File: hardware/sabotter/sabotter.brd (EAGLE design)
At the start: 100 x 80 mm, 96 parts, among them IC1 MAX3232CSE, IC2 MAX3232CSE, IC3 OKI-78SR-3.3/1.5-W36H-C, IC4 OKI-78SR-5/1.5-W36H-C, IC6 ATXMEGA256A3U-AU

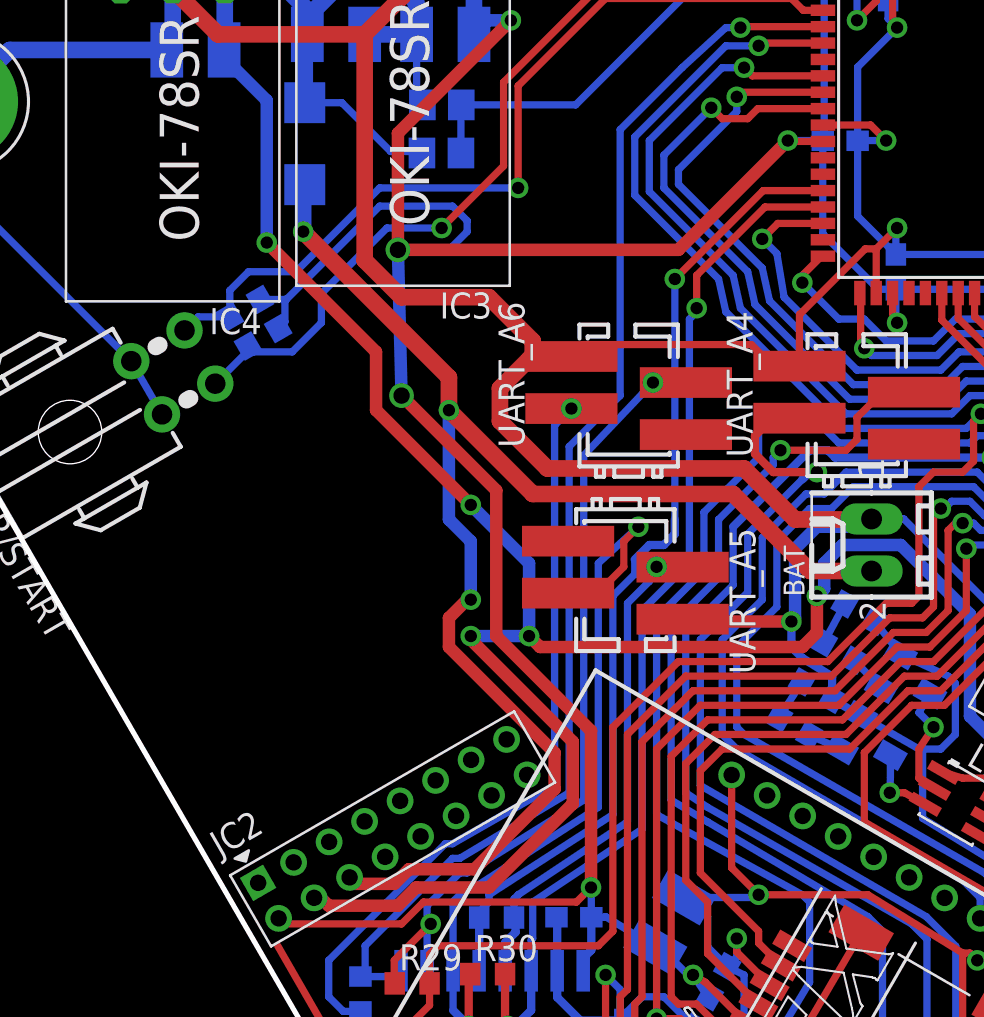
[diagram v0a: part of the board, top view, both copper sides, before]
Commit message: add audio amplifier
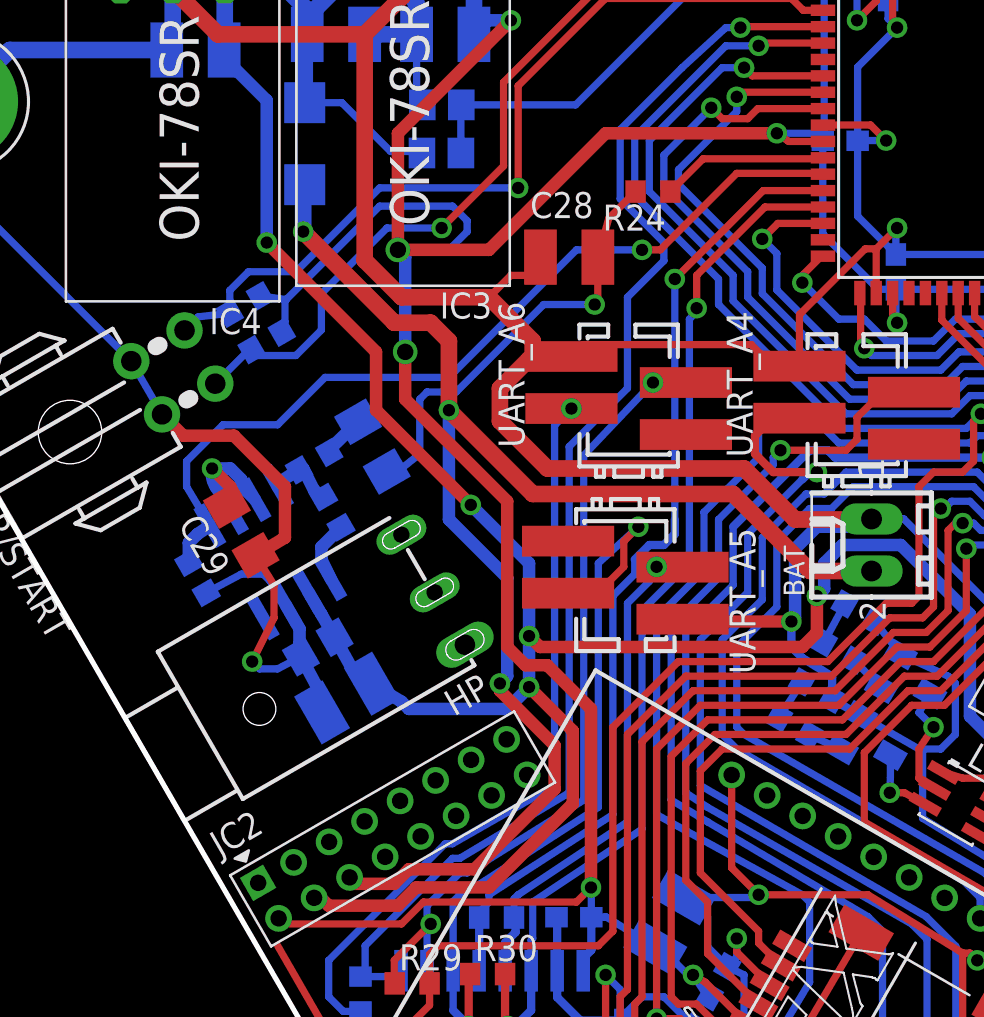
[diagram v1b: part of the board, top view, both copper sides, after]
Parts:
- added C27, C29: 1UF_50V_1206, robotter_capacitor:C1206
- added C28, C30: C_10UF, robotter_capacitor:C1210
- added C31: 100NF_50V_0805, robotter_capacitor:C0805
- added HP: 1503_04, con-lumberg:1503_04
- added IC7: LM4871M, robotter_ic:SO8
- added R24, R25, R37, R38: 10K-F, robotter_resistor:R0603
- C13, C14, C15, C16, C2: value 10UF35V-C -> 10UFC
- moved R2 0.25 mm to (23.3, 60.1)
- moved R3 0.18 mm to (22.2, 61.9)
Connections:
- new net AUDIO_PWM_3V3: IC6.26, R24.1
- new net ENABLE_AUDIO_OUPUT_3V3: IC6.27, IC7.1, R38.2
- new net N$15: C29.2, IC7.2, IC7.3
- new net N$20: C27.1, C28.2, R24.2
- new net N$36: C27.2, R25.1
- new net N$37: IC7.4, R25.2, R37.1
- new net N$38: IC7.5, R37.2
- net +5V: now also C30.1, C31.1, IC7.6
- net GND: now also C28.1, C29.1, C30.2, C31.2, IC7.7, R38.1
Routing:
- net ENABLE_AUDIO_OUPUT_3V3: track 0.00 -> 42.7 mm, vias 0 -> 1
- net GND: track 512.6 -> 546.9 mm, vias 18 -> 19
- net N$20: track 0.00 -> 21.2 mm, vias 0 -> 1
- net +5V: track 113.5 -> 123.6 mm
- net AUDIO_PWM_3V3: track 0.00 -> 8.13 mm
- net N$15: track 0.00 -> 7.57 mm, vias 0 -> 1
- net N$37: track 0.00 -> 3.37 mm
- net N$38: track 0.00 -> 3.02 mm
- net N$36: track 0.00 -> 2.11 mm
- net +3V3: track 259.8 -> 261.7 mm
- net RX_A6_3V3: track 62.3 -> 64.0 mm

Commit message: board ready for eirbot assembly
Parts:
- removed LED3, LED4, LED5: GREEN_0805, robotter_diode:CHIP-LED0805
- added LA1, LA3, LA4: GREEN_0805, robotter_diode:CHIP-LED0805
- added R39, R40, R41, R42: 10K-F, robotter_resistor:R0603
- moved LED9 61.7 mm to (4.17, 67.8), turned to 30 degrees
- moved LED6 60.5 mm to (9.40, 60.3)
- moved LED7 60.5 mm to (8.14, 62.7)
- moved LED8 60.5 mm to (6.91, 65.0)
- moved R8 59.4 mm to (14.4, 61.5), turned to 180 degrees
- moved R10 59.1 mm to (11.8, 65.8), turned to 180 degrees
- moved R9 59.0 mm to (13.1, 63.7), turned to 180 degrees
- moved R11 57.8 mm to (13.2, 67.9), turned to 180 degrees
- moved R5 1.83 mm to (70.7, 41.7)
- moved R4 1.12 mm to (72.9, 43.7)
- moved R6 0.40 mm to (68.4, 33.5)
- moved R7 0.18 mm to (67.0, 31.1)
- renumbered LED2 to LA2, UART_A4 to UART_E0, UART_A5 to UART_D0, UART_A6 to UART_C0
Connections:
- net RX_A4_232 renamed RX_E0_232
- net RX_A5_232 renamed RX_D0_232
- net RX_A6_232 renamed RX_C0_232
- net TX_A4_232 renamed TX_E0_232
- net TX_A4_3V3 renamed TX_E0_3V3
- net TX_A5_232 renamed TX_D0_232
- net TX_A5_3V3 renamed TX_D0_3V3
- net TX_A6_232 renamed TX_C0_232
- net TX_A6_3V3 renamed TX_C0_3V3
- removed net N$10: LED4.A
- removed net N$11: LED7.C, R9.2
- removed net N$12: LED5.A
- removed net N$74: IC6.1
- removed net N$77: IC6.2
- removed net N$78: IC6.3
- removed net N$79: IC6.4
- removed net N$80: IC6.5
- removed net N$9: LED3.A
- removed net RX_A4_3V3: IC1.12, IC6.38, R26.2
- removed net RX_A5_3V3: IC2.12, IC6.28, R27.2
- removed net RX_A6_3V3: IC2.9, IC6.18, R28.2
- new net LA1: IC6.63, R5.2
- new net LA2: IC6.64, R4.2
- new net LA3: IC6.1, R7.2
- new net LA4: IC6.2, R6.2
- new net RX_C0_3V3: IC2.9, IC6.18, R28.2, R39.2
- new net RX_D0_3V3: IC2.12, IC6.28, R27.2, R40.2
- new net RX_E0_3V3: IC1.12, IC6.38, R26.2, R41.2
- net GND: now also LA1.C, LA2.C, LA3.C, LA4.C, LED6.C, LED7.C, LED8.C, LED9.C, R39.1, R40.1, R41.1, R42.1; no longer R10.1, R11.1, R4.1, R5.1, R6.1, R7.1, R8.1, R9.1
- net N$1: now also LA2.A, R4.1; no longer LA2.C, R4.2
- net N$13: now also R8.2; no longer LED6.A
- net N$14: now also R9.2; no longer LED7.A
- net N$16: now also R10.2; no longer LED8.A
- net N$17: now also R11.2; no longer LED9.A
- net N$2: now also LA1.A, R5.1; no longer LED3.C, R5.2
- net N$3: now also LED6.A, R8.1; no longer LED4.C, R6.2
- net N$4: now also LA3.A, R7.1; no longer LED5.C, R7.2
- net N$5: now also LED7.A, R9.1; no longer LED6.C, R8.2
- net N$6: now also LED8.A, R10.1; no longer LED8.C, R10.2
- net N$7: now also LED9.A, R11.1; no longer LED9.C, R11.2
- net N$8: now also LA4.A, R6.1; no longer LA2.A
- net RX_PROP_3V3: now also R42.2
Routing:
- net LA3: track 0.00 -> 70.5 mm, vias 0 -> 1
- net LA4: track 0.00 -> 69.9 mm, vias 0 -> 1
- net RX_C0_3V3: track 0.00 -> 66.7 mm, vias 0 -> 1
- net RX_A6_3V3: track 64.0 -> 0.00 mm, vias 1 -> 0
- net RX_E0_3V3: track 0.00 -> 60.9 mm, vias 0 -> 1
- net RX_A4_3V3: track 60.6 -> 0.00 mm, vias 1 -> 0
- net LA1: track 0.00 -> 53.0 mm, vias 0 -> 1
- net LA2: track 0.00 -> 52.2 mm, vias 0 -> 1
- net RX_D0_3V3: track 0.00 -> 48.4 mm, vias 0 -> 1
- net RX_A5_3V3: track 47.9 -> 0.00 mm, vias 1 -> 0
- net GND: track 546.9 -> 584.4 mm, vias 19 -> 23
- net N$2: track 0.00 -> 7.28 mm, vias 0 -> 1
- net RX_PROP_3V3: track 24.7 -> 29.9 mm
- net N$7: track 3.59 -> 8.28 mm
- net N$1: track 0.00 -> 3.58 mm, vias 0 -> 1
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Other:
- board text added: "Sab'Otter V1"

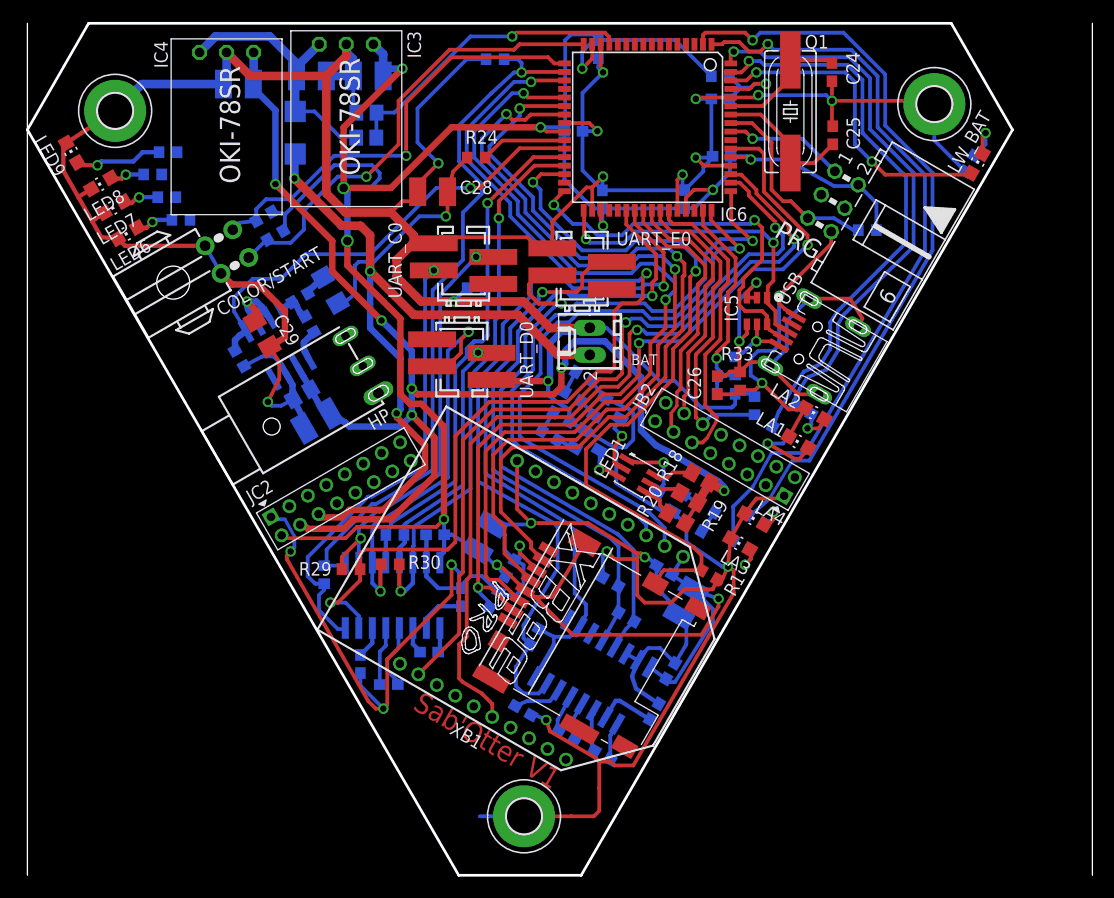
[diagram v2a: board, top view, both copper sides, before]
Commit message: board ready for eirbot assembly, sabotter V1
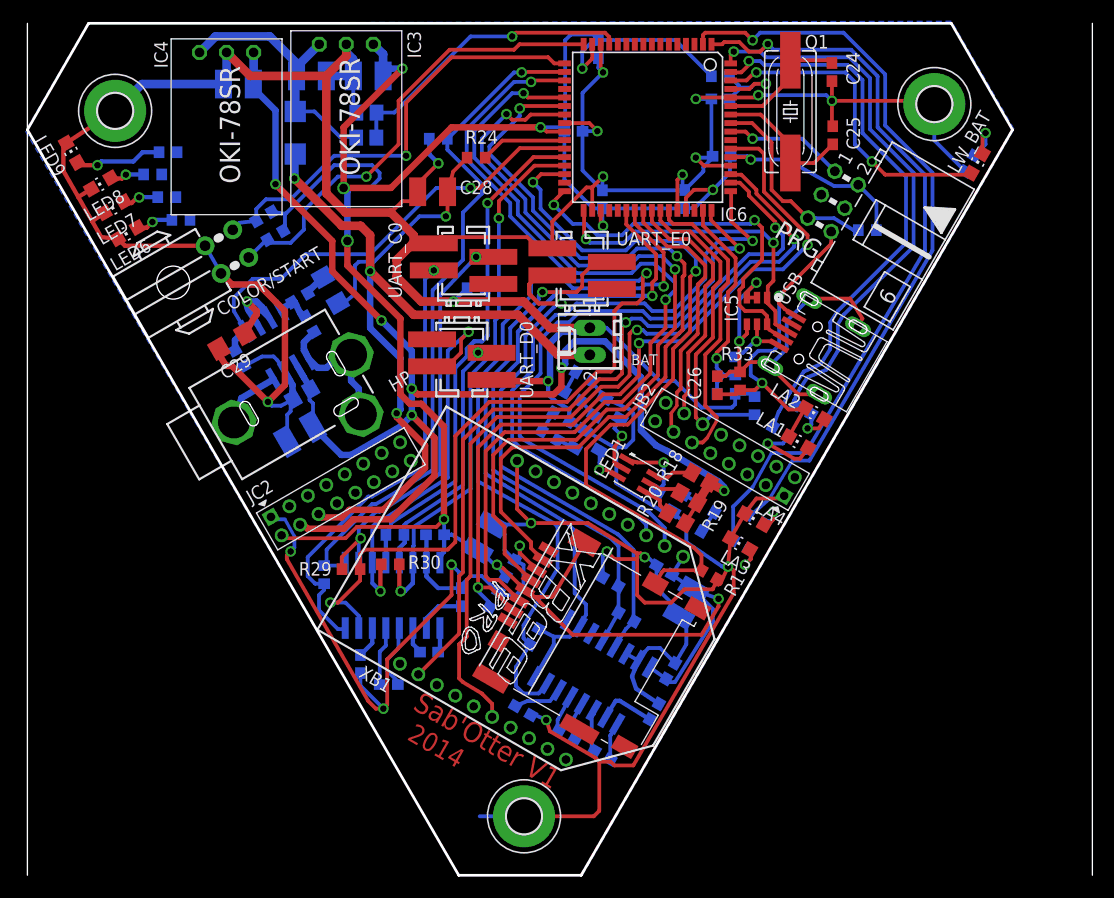
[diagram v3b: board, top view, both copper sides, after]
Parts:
- HP: value 1503_04 -> 1503_12"; device con-lumberg:1503_04 -> robotter_connector:1503_12
- moved R39 9.18 mm to (38.6, 69.2)
- moved HP 4.06 mm to (24.9, 45.7)
- moved C29 2.93 mm to (19.2, 50.1), turned to 30 degrees
- moved C30 2.03 mm to (25.6, 41.4)
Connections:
- net N$13 renamed LED4
- net N$14 renamed LED3
- net N$16 renamed LED2
- net N$17 renamed LED1
- new net N$9: HP.5, IC7.8
- net N$38: now also HP.3, HP.4
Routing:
- net N$38: track 3.02 -> 13.8 mm
- net N$9: track 0.00 -> 5.91 mm
- net GND: track 584.4 -> 580.5 mm
- net +5V: track 123.6 -> 127.3 mm
- net RX_C0_3V3: track 66.7 -> 65.1 mm
- net N$15: track 7.57 -> 9.04 mm
- added copper zone on layer 1, net GND
- added copper zone on layer 16, net GND
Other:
- board text added: "2014"

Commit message: leds connected to µC, board ready for industrial assembly, sabotter V2
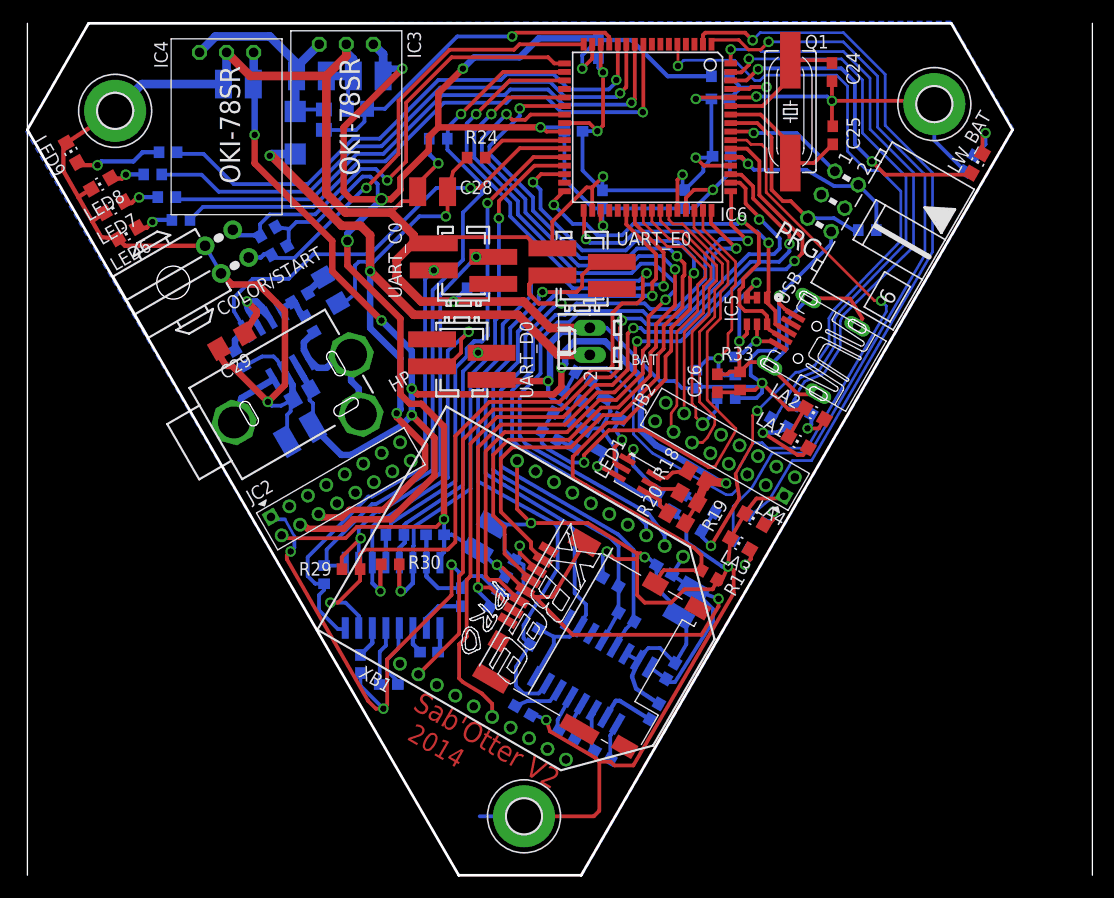
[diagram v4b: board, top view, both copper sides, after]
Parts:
- moved R23 4.32 mm to (27.8, 71.0), turned to 90 degrees
- moved R35 3.11 mm to (62.8, 46.6), turned to 90 degrees
- moved R42 2.76 mm to (65.6, 44.8), turned to 0 degrees
- moved R2 1.47 mm to (23.6, 58.7)
- moved R3 1.47 mm to (22.6, 60.5)
- moved R22 0.96 mm to (30.9, 72.0)
- moved R5 0.83 mm to (70.6, 42.5)
- moved R18 0.40 mm to (62.9, 37.5)
- moved C26 0.18 mm to (64.8, 46.2)
- moved USB 0.09 mm to (78.8, 46.8)
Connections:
- net LA1 renamed LA1_3V3
- net LA2 renamed LA2_3V3
- net LA3 renamed LA3_3V3
- net LA4 renamed LA4_3V3
- removed net LED1: R11.2
- removed net LED2: R10.2
- removed net LED3: R9.2
- removed net LED4: R8.2
- removed net N$112: IC6.55
- removed net N$54: R12.1, R17.2
- removed net N$55: R13.1, R16.2
- removed net N$56: R14.1, R15.2
- removed net N$81: IC6.6
- removed net N$82: IC6.7
- removed net N$83: IC6.8
- removed net N$84: IC6.9
- removed net N$85: IC6.10
- removed net N$86: IC6.11
- removed net N$87: IC6.12
- new net LB3_3V3: IC6.9, R8.2
- new net LB4_3V3: IC6.10, R9.2
- new net LB5_3V3: IC6.11, R10.2
- new net LB6_3V3: IC6.12, R11.2
- new net LED_BLUE_3V3: IC6.5, R12.1, R17.2
- new net LED_GREEN_3V3: IC6.55, R13.1, R16.2
- new net LED_RED_3V3: IC6.46, R14.1, R15.2
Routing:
- net LED_BLUE_3V3: track 0.00 -> 76.7 mm, vias 0 -> 3
- net LED_GREEN_3V3: track 0.00 -> 73.1 mm, vias 0 -> 1
- net LB3_3V3: track 0.00 -> 54.3 mm, vias 0 -> 1
- net LB5_3V3: track 0.00 -> 53.6 mm, vias 0 -> 1
- net LB4_3V3: track 0.00 -> 53.4 mm, vias 0 -> 1
- net LB6_3V3: track 0.00 -> 51.2 mm, vias 0 -> 1
- net LED_RED_3V3: track 0.00 -> 50.5 mm, vias 0 -> 1
- net +3V3: track 261.7 -> 269.8 mm, vias 11 -> 12
- net GND: track 580.5 -> 576.4 mm
- net N$62: track 25.9 -> 22.0 mm
- net VBAT_0_1V: track 28.2 -> 32.0 mm
- net +12V: track 71.9 -> 75.4 mm
- net RX_PROP_3V3: track 29.9 -> 27.3 mm
- net N$55: track 2.14 -> 0.00 mm
- net N$54: track 2.14 -> 0.00 mm
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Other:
- board text added: "Sab'Otter V2"
- board text removed: "Sab'Otter V1"

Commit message: led inverted, now in ascending order
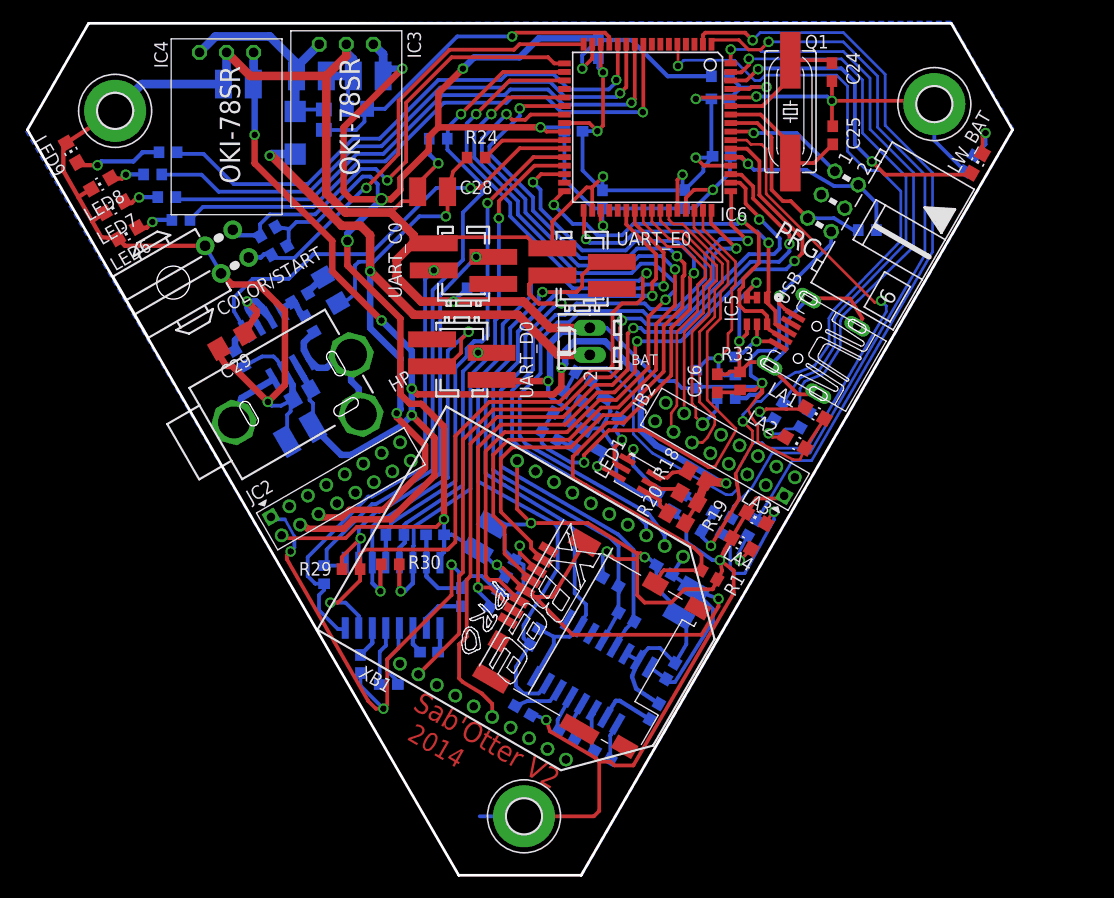
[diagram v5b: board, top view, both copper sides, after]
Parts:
- moved LA2 3.30 mm to (72.1, 40.6), turned to 240 degrees
- moved LA1 3.14 mm to (73.9, 43.4), turned to 240 degrees
- moved LA3 2.88 mm to (68.5, 33.5)
- moved LA4 2.59 mm to (67.1, 31.2)
- moved R7 2.22 mm to (65.7, 32.8), turned to 120 degrees
- moved R5 1.08 mm to (70.5, 43.6), turned to 120 degrees
- moved R4 0.93 mm to (73.0, 42.8), turned to 120 degrees
- moved R6 0.92 mm to (68.0, 32.6), turned to 120 degrees
- moved R12 0.15 mm to (63.6, 34.5)
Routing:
- net N$4: track 3.44 -> 13.1 mm
- net GND: track 576.4 -> 583.1 mm
- net LA3_3V3: track 71.1 -> 69.1 mm
- net LA1_3V3: track 52.9 -> 50.9 mm
- net N$1: track 3.58 -> 5.18 mm
- net N$2: track 7.85 -> 6.61 mm
- net LED_BLUE_3V3: track 76.7 -> 77.8 mm
- net LA2_3V3: track 52.7 -> 53.7 mm
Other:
- board size 100 x 80 mm -> 92.5 x 80 mm
